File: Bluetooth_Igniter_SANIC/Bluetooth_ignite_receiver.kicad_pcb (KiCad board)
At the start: 2 copper layers, 65 parts, among them J1 Screw_Terminal_01x02, J2 Screw_Terminal_01x02, J3 Screw_Terminal_01x02, J4 Screw_Terminal_01x02, J5 USB_C_Receptacle_USB2.0, Q1 MMDT2222A, Q2 MMDT2222A, Q3 Q_NMOS_GSD, Q4 Q_NMOS_GSD, SW1 SW_Push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

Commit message: Separate voltage supply for ESP32 and pyros
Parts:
- added D12: TX_LED, LED_SMD:LED_0603_1608Metric_Castellated, F.Cu at (43.8, 89.7)
- added D13: RX_LED, LED_SMD:LED_0603_1608Metric_Castellated, F.Cu at (43.8, 88.1)
- added R24: 470, Resistor_SMD:R_0603_1608Metric, F.Cu at (40.4, 89.8)
- added R25: 470, Resistor_SMD:R_0603_1608Metric, F.Cu at (40.4, 88.1)
- moved R8 220.2 mm to (48.3, 93.3), turned to 270 degrees
- moved D2 195.0 mm to (56.7, 90.2), turned to 180 degrees
- moved D1 184.6 mm to (62.4, 85.3), turned to 90 degrees
- moved R5 184.4 mm to (56.7, 82.2), turned to 180 degrees
- moved U1 183.4 mm to (56.7, 85.6), turned to 180 degrees
- moved Q1 182.1 mm to (57.4, 109.6)
- moved Q2 182.1 mm to (53.3, 109.6)
- moved R1 182.1 mm to (57.4, 111.8)
- moved R2 182.1 mm to (53.3, 111.9)
- moved R3 169.2 mm to (60.3, 83.7), turned to 270 degrees
- moved R4 166.6 mm to (60.2, 86.8), turned to 270 degrees
- moved D11 148.4 mm to (67.5, 83.2), turned to 90 degrees
- moved J5 142.6 mm to (72.8, 88.0), turned to 270 degrees
- moved D10 142.4 mm to (76.8, 81.6), turned to 180 degrees
- moved R23 141.5 mm to (70.2, 81.7), turned to 180 degrees
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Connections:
- U2 pad 34: /TXD -> Net-(R24-Pad1)
- U2 pad 35: /RXD -> Net-(R25-Pad1)
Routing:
- net +3V3: track 8.40 -> 32.6 mm
- net /usb/D-: track 0.00 -> 19.8 mm
- net Net-(D5-Pad1): track 0.00 -> 18.9 mm
- net Net-(D8-Pad1): track 0.00 -> 18.8 mm
- net /EN: track 0.00 -> 15.1 mm
- net Net-(J5-PadB5): track 0.00 -> 12.7 mm
- net Net-(J5-PadA5): track 0.00 -> 11.8 mm
- net Net-(D8-Pad2): track 0.00 -> 11.2 mm
- net Net-(D5-Pad2): track 0.00 -> 10.7 mm
- net GND: track 21.8 -> 12.0 mm
- net /usb/D+: track 0.00 -> 8.08 mm
- net Net-(D9-Pad1): track 0.00 -> 7.85 mm, vias 0 -> 2
- net Net-(C5-Pad1): track 0.00 -> 7.64 mm
- net Net-(C4-Pad1): track 0.00 -> 7.64 mm
- net Net-(D6-Pad1): track 0.00 -> 6.54 mm, vias 0 -> 2
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
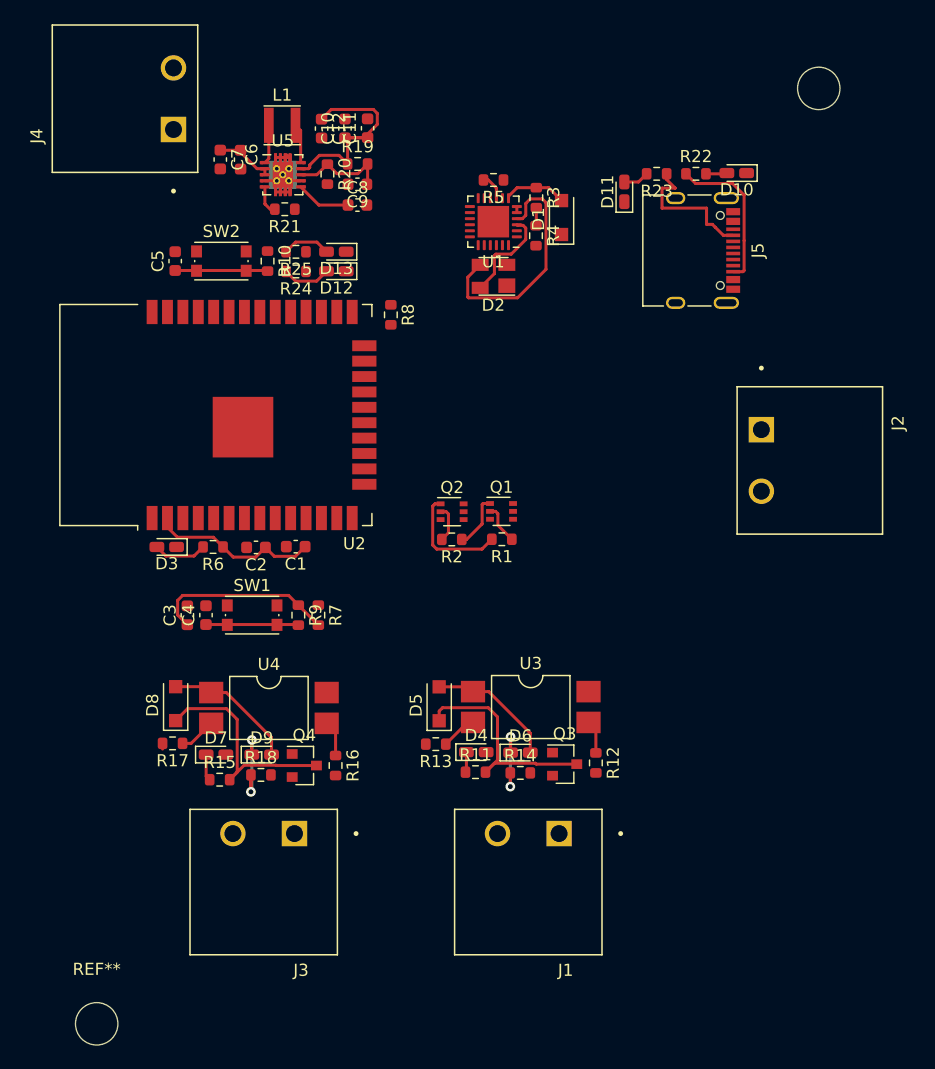
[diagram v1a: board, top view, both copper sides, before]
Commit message: small schematic changes
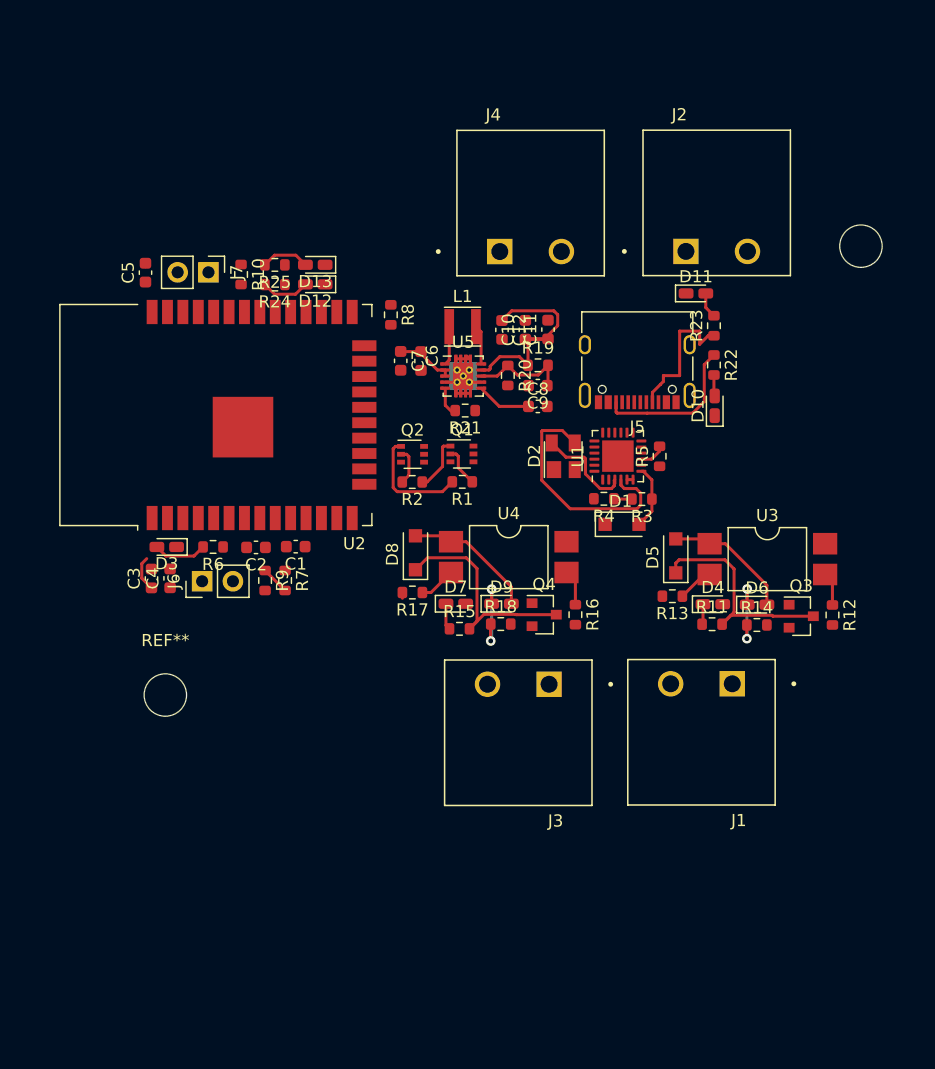
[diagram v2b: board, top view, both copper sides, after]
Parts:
- removed SW1, SW2: SW_Push, Button_Switch_SMD:SW_Push_1P1T_NO_CK_KMR2
- added J6: Conn_01x02_Male, Connector_PinHeader_2.54mm:PinHeader_1x02_P2.54mm_Vertical, F.Cu at (32.7, 115.3)
- added J7: Conn_01x02_Male, Connector_PinHeader_2.54mm:PinHeader_1x02_P2.54mm_Vertical, F.Cu at (33.2, 89.8)
- moved J4 34.6 mm to (59.8, 84.1), turned to 0 degrees
- moved REF** 27.7 mm to (29.7, 124.7)
- moved R5 26.6 mm to (70.4, 105.0), turned to 90 degrees
- moved R3 26.3 mm to (69.0, 108.5), turned to 180 degrees
- moved D1 25.8 mm to (67.3, 110.6), turned to 0 degrees
- moved J3 24.4 mm to (58.8, 127.8)
- moved D7 23.4 mm to (53.6, 117.2)
- moved D9 23.4 mm to (57.4, 117.2)
- moved Q4 23.4 mm to (60.9, 118.1)
- moved R16 23.4 mm to (63.5, 118.1)
- moved R17 23.4 mm to (50.1, 116.2)
- moved R18 23.4 mm to (57.3, 118.8)
- moved U4 23.4 mm to (58.0, 113.3)
- moved D8 23.4 mm to (50.3, 113.0)
- moved R15 23.4 mm to (53.9, 119.2)
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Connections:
- J2 pad 1: VDD -> GND
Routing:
- net +3V3: track 32.6 -> 19.2 mm
- net /EN: track 15.1 -> 5.25 mm
- net Net-(C5-Pad1): track 7.64 -> 0.07 mm
- net Net-(C4-Pad1): track 7.64 -> 0.07 mm

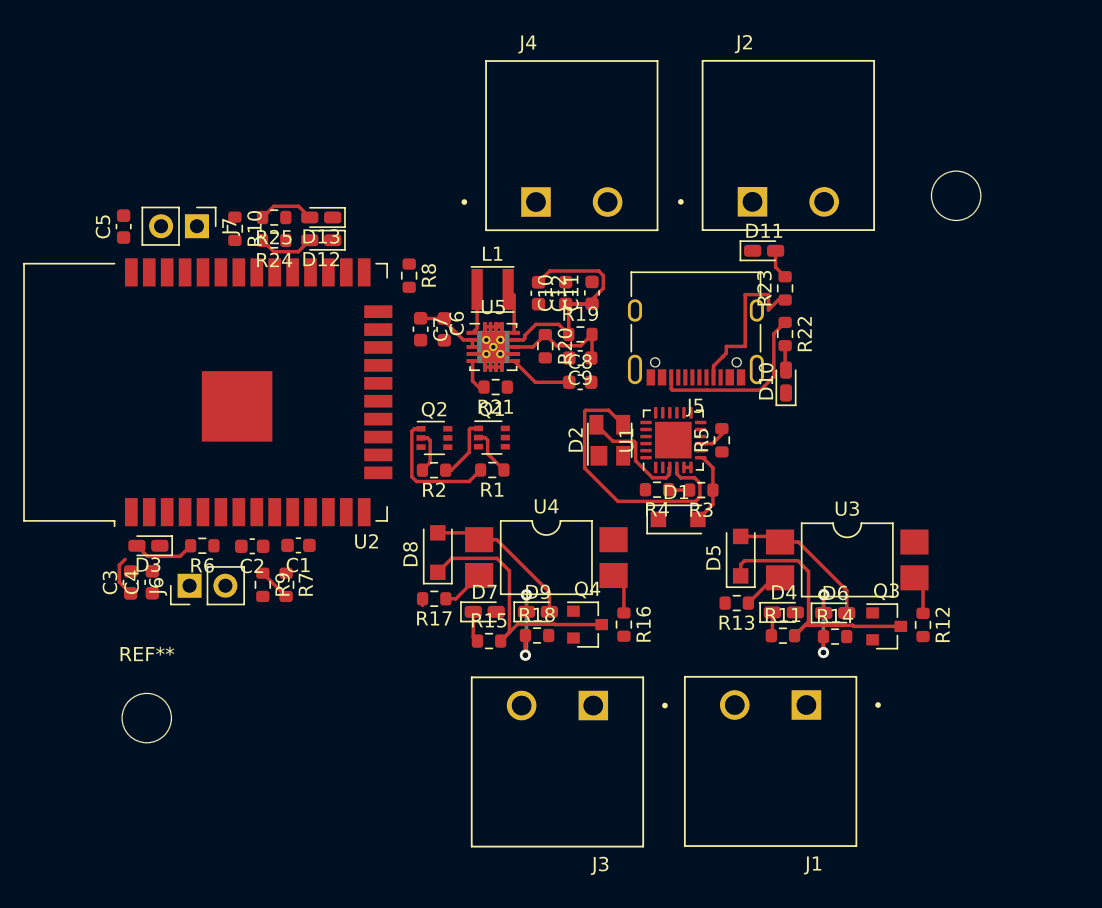
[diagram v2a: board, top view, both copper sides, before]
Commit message: smaller mounting holes
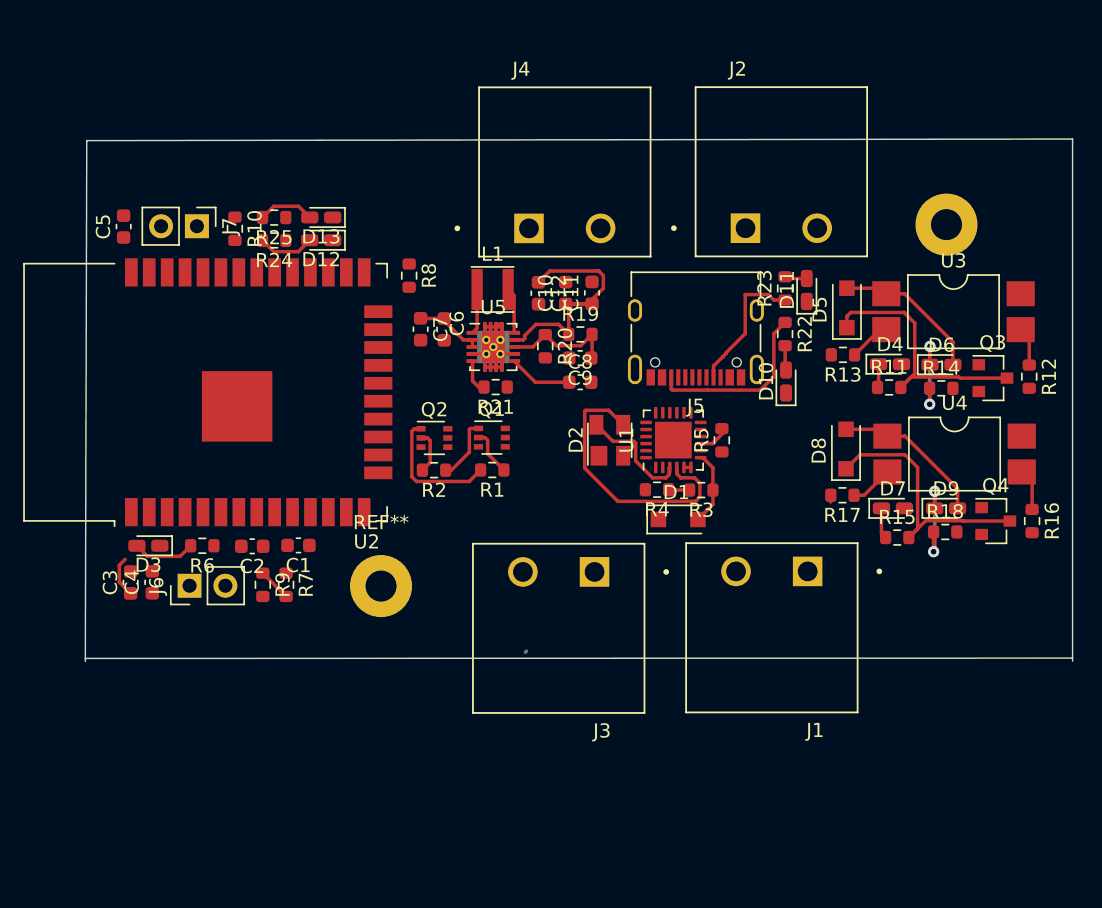
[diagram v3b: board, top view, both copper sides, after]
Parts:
- REF** (x2): value MountingHole_3.5mm -> MountingHole_2.2mm_M2_Pad; footprint MountingHole:MountingHole_3.5mm -> MountingHole:MountingHole_2.2mm_M2_Pad
- moved D8 29.9 mm to (79.2, 105.6)
- moved R15 29.9 mm to (82.9, 111.9)
- moved D7 29.9 mm to (82.6, 109.8)
- moved Q4 29.9 mm to (89.9, 110.7)
- moved R17 29.9 mm to (79.0, 108.9)
- moved R18 29.9 mm to (86.3, 111.5)
- moved U4 29.9 mm to (86.9, 106.0)
- moved D9 29.9 mm to (86.3, 109.8)
- moved R16 29.9 mm to (92.4, 110.7)
- moved R11 19.1 mm to (82.3, 101.3)
- moved D4 19.1 mm to (82.4, 99.6)
- moved Q3 19.1 mm to (89.7, 100.6)
- moved R14 19.1 mm to (86.0, 101.3)
- moved D5 19.1 mm to (79.3, 95.6)
- moved D6 19.1 mm to (86.0, 99.6)
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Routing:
- net Net-(J5-PadA5): track 11.8 -> 9.79 mm
- net Net-(D11-Pad2): track 2.12 -> 1.61 mm
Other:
- board outline added: 70 x 37 mm

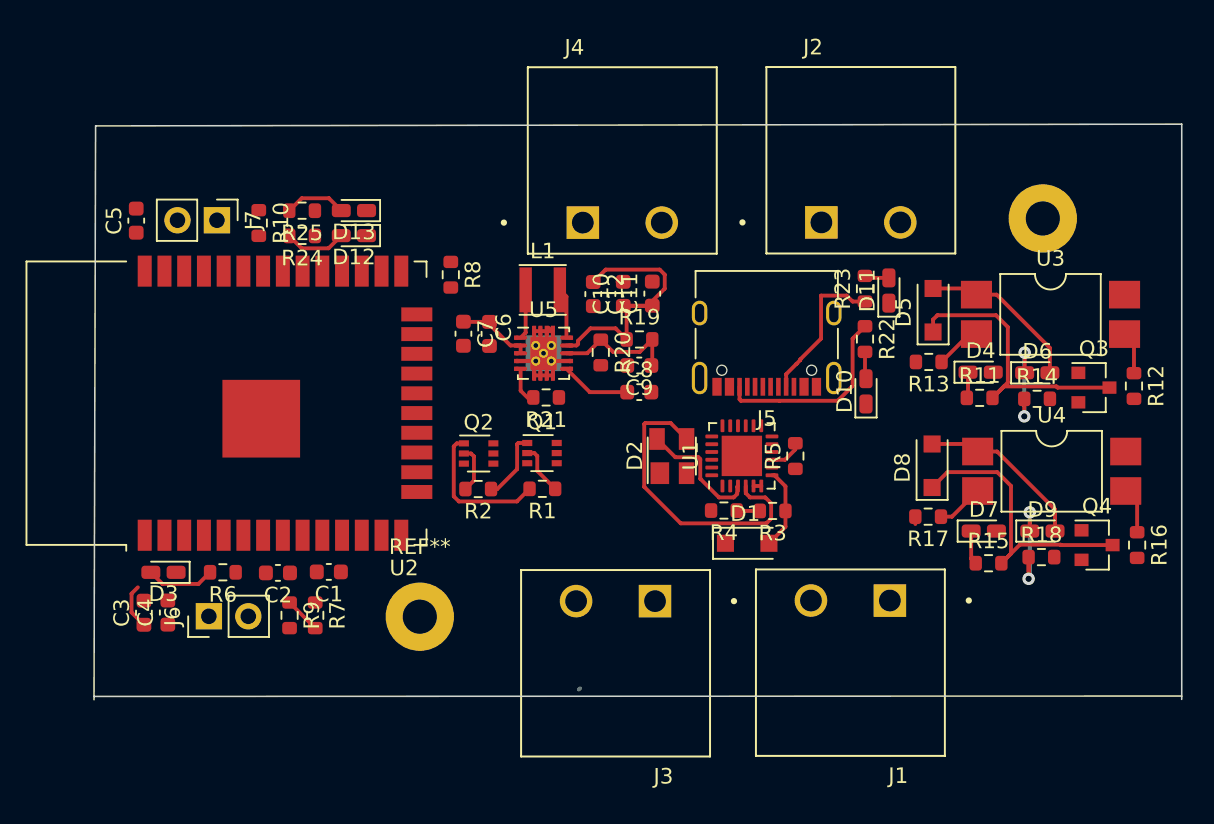
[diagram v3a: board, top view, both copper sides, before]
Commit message: resized pcb
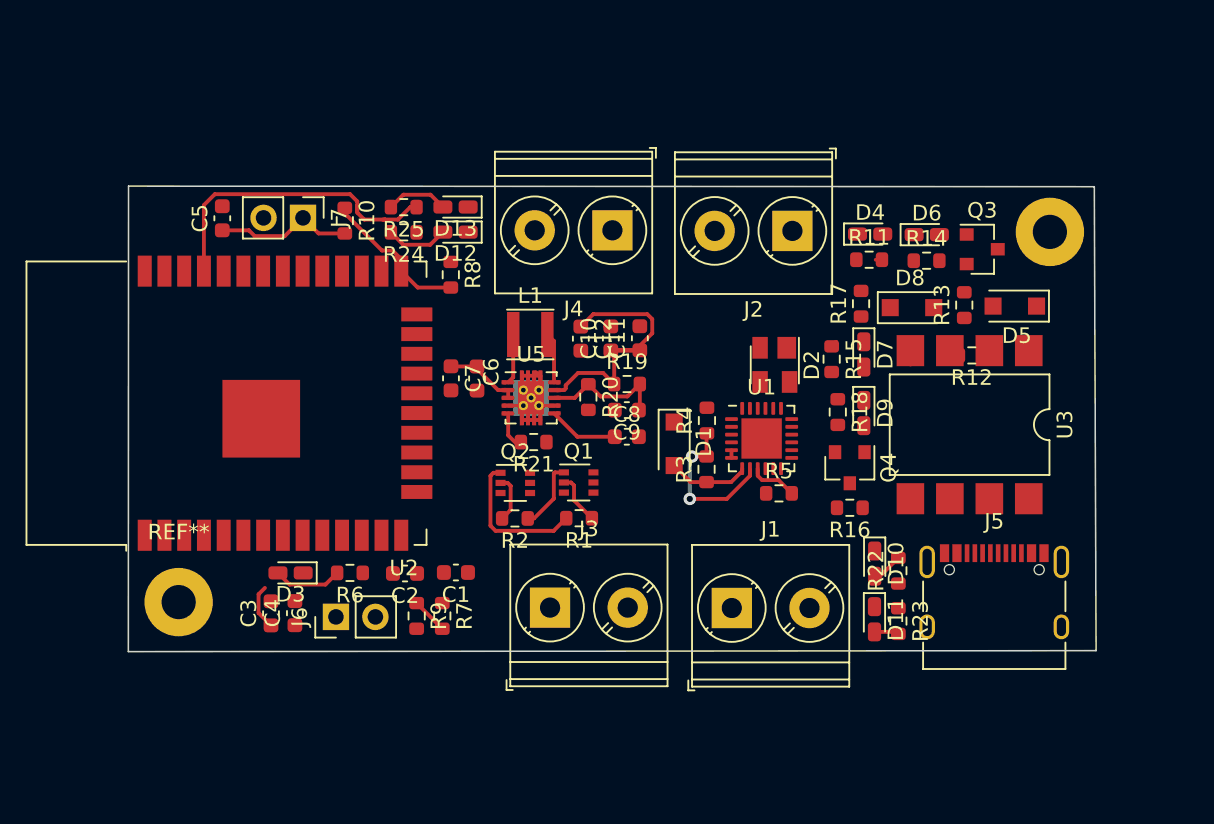
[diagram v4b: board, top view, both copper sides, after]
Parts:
- removed U4: LTV-817S, Package_DIP:SMDIP-4_W9.53mm
- J1, J2, J3, J4: footprint iclrhw:PHOENIX_1757242 -> TerminalBlock_Phoenix:TerminalBlock_Phoenix_PT-1,5-2-5.0-H_1x02_P5.00mm_Horizontal
- U3: value LTV-817S -> LTV-827S; footprint Package_DIP:SMDIP-4_W9.53mm -> Package_DIP:SMDIP-8_W9.53mm
- moved J5 23.2 mm to (83.2, 114.9), turned to 0 degrees
- moved R23 21.5 mm to (77.1, 115.6), turned to 270 degrees
- moved D11 21.2 mm to (75.5, 115.5), turned to 270 degrees
- moved R16 18.6 mm to (74.0, 108.3), turned to 180 degrees
- moved Q4 16.7 mm to (74.0, 105.8), turned to 270 degrees
- moved R15 16.6 mm to (72.8, 98.8), turned to 270 degrees
- moved R18 16.1 mm to (73.2, 102.2), turned to 270 degrees
- moved REF** 15.5 mm to (30.8, 114.4)
- moved R22 15.1 mm to (77.1, 112.4), turned to 90 degrees
- moved R17 14.4 mm to (74.7, 95.2), turned to 90 degrees
- moved D9 13.8 mm to (74.9, 102.2), turned to 270 degrees
- moved D7 13.7 mm to (74.9, 98.5), turned to 270 degrees
- moved Q3 11.4 mm to (82.5, 91.7)
- moved D4 11.4 mm to (75.3, 90.7)
- moved R14 11.4 mm to (78.9, 92.4)
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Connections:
- U3 pad 1: Net-(D5-Pad2) -> +3V3
- U3 pad 2: Net-(R13-Pad1) -> /Cont1
- U3 pad 3: /Cont1 -> +3V3
- U3 pad 4: +3V3 -> /Cont2
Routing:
- net Net-(R25-Pad1): track 0.00 -> 20.2 mm
- net /usb/D-: track 19.8 -> 0.00 mm
- net Net-(D8-Pad1): track 18.8 -> 0.00 mm
- net Net-(D5-Pad1): track 18.9 -> 0.40 mm
- net Net-(J5-PadB5): track 12.7 -> 0.00 mm
- net Net-(D8-Pad2): track 11.2 -> 0.00 mm
- net Net-(D5-Pad2): track 10.7 -> 0.00 mm
- net Net-(J5-PadA5): track 9.79 -> 0.00 mm
- net /BOOT: track 0.00 -> 9.60 mm
- net Net-(C5-Pad1): track 0.07 -> 9.01 mm
- net Net-(R3-Pad2): track 1.50 -> 10.2 mm, vias 0 -> 2
- net /usb/D+: track 8.08 -> 0.00 mm
- net Net-(D9-Pad1): track 7.85 -> 0.11 mm, vias 2 -> 0
- net Net-(D6-Pad1): track 6.54 -> 0.00 mm, vias 2 -> 0
- net Net-(R13-Pad1): track 2.99 -> 0.00 mm
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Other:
- board size 70 x 37 mm -> 62.3 x 30 mm
